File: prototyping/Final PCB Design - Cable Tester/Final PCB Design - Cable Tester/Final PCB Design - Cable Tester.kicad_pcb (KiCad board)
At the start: 2 copper layers, 86 x 54 mm, 41 parts, among them J17 Banana Jack, J20 SFML-110-02-L-D-A, J3 Debug Connection, J4 MEM2061-01-188-00-A_REVA, J5 Barrel Jack 9V, J6 Touchscreen HMI, Q1 2N3904, SW1 Rocker Switch, U1 AVR128DB64x-xMR, U2 LP2985-3.3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

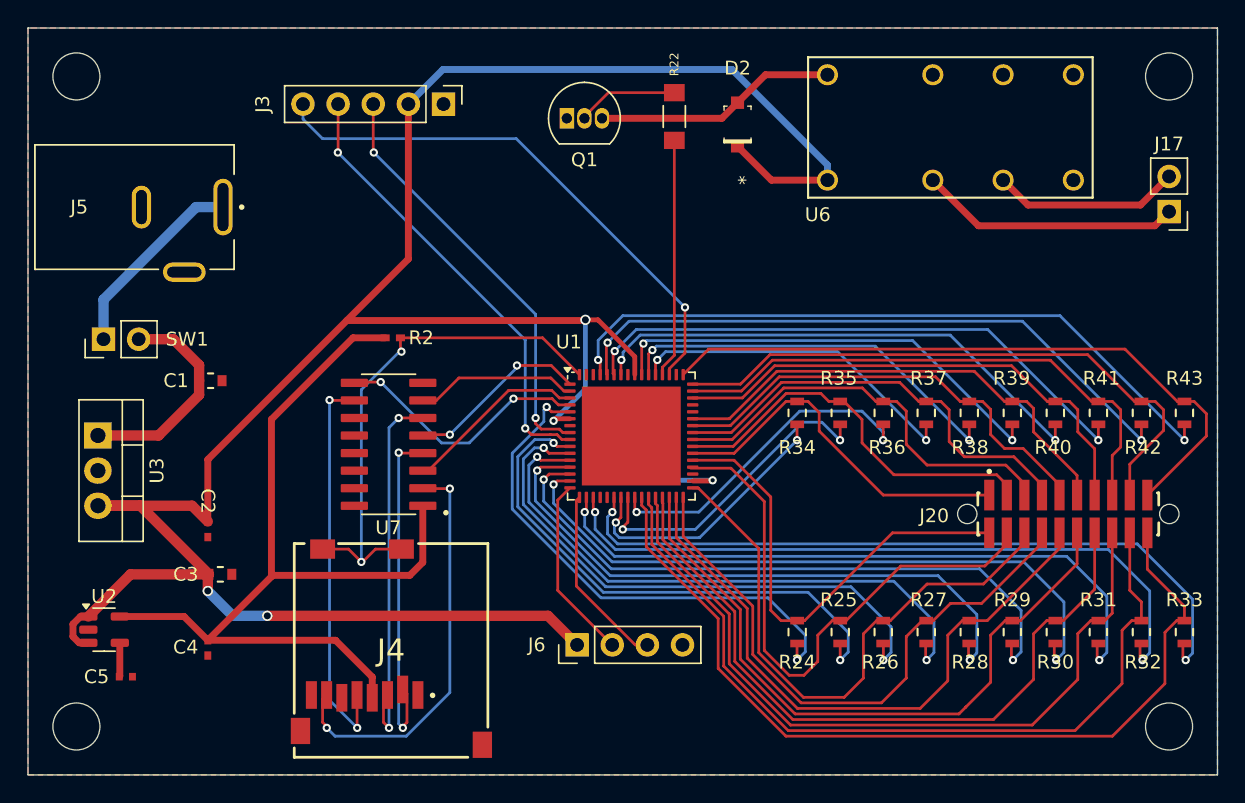
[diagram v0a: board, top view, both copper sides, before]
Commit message: Update - Final PCB to JLCPCB components
Added the JLCPCB Library and updated to equivalent components supplied by JLCPCB. Also updated the PCB traces to fit new components.
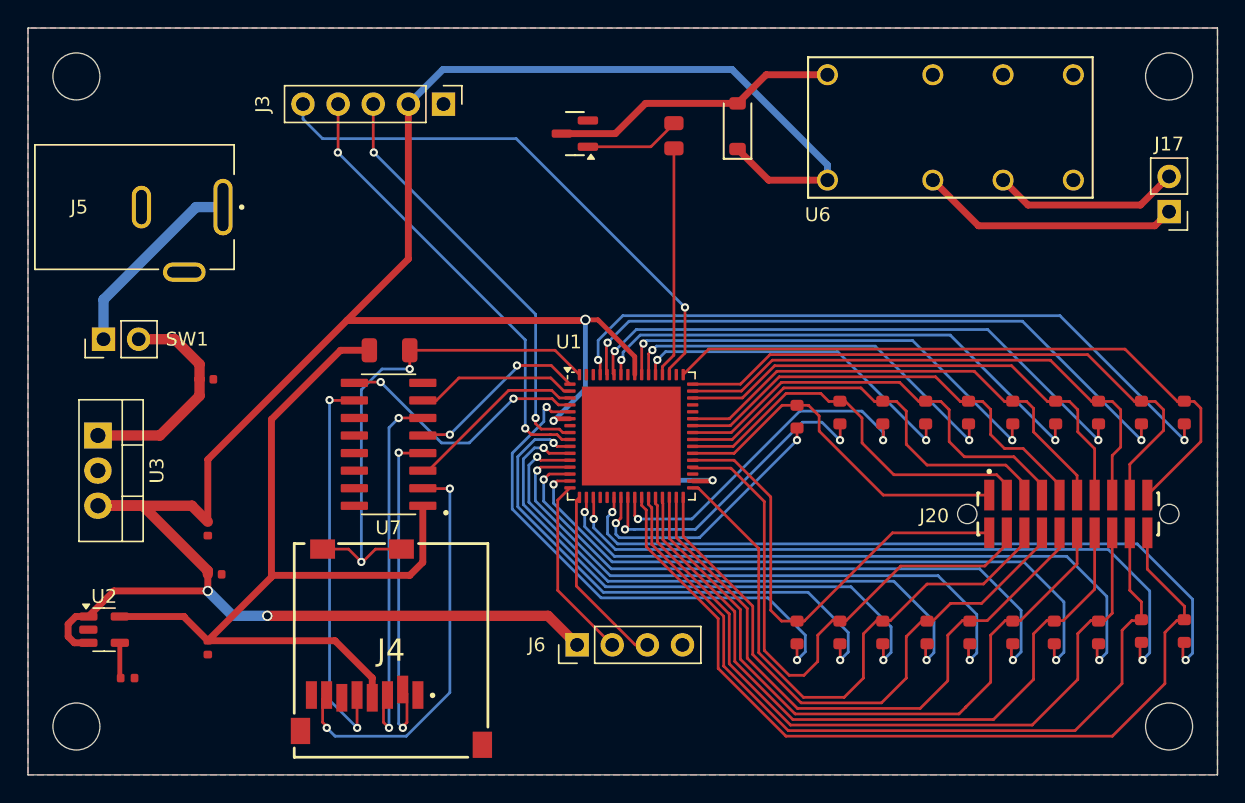
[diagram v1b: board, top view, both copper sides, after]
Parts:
- removed D2: 1N4148W-TP, digikey-footprints:SOD-123
- removed Q1: 2N3904, Package_TO_SOT_THT:TO-92_Inline
- removed R24, R25, R26, R27, R28, R29, R30, R31, R32, R33, R34, R35, R36, R37, R38, R39, R40, R41, R42, R43: 1kΩ ±0.1% 0.1W, KiCad Symbols and Footprints:RES_0816_SUS
- added D1: 1N4148W, PCM_JLCPCB:D_SOD-123, F.Cu at (142.8, 73.1)
- added Q2: MMBT3904, PCM_JLCPCB:Q_SOT-23, F.Cu at (131.0, 73.6)
- added R1: 10kΩ, PCM_JLCPCB:R_1206, F.Cu at (117.6, 89.3)
- added R10: 1kΩ ±0.1% 0.1W, PCM_JLCPCB:R_0603, F.Cu at (168.9, 109.7)
- added R11: 1kΩ ±0.1% 0.1W, PCM_JLCPCB:R_0603, F.Cu at (172.0, 109.6)
- added R12: 1kΩ ±0.1% 0.1W, PCM_JLCPCB:R_0603, F.Cu at (175.1, 109.6)
- added R13: 1kΩ ±0.1% 0.1W, PCM_JLCPCB:R_0603, F.Cu at (147.1, 94.1)
- added R14: 1kΩ ±0.1% 0.1W, PCM_JLCPCB:R_0603, F.Cu at (150.2, 93.8)
- added R15: 1kΩ ±0.1% 0.1W, PCM_JLCPCB:R_0603, F.Cu at (153.3, 93.8)
- added R16: 1kΩ ±0.1% 0.1W, PCM_JLCPCB:R_0603, F.Cu at (156.4, 93.8)
- added R17: 1kΩ ±0.1% 0.1W, PCM_JLCPCB:R_0603, F.Cu at (159.5, 93.8)
- added R18: 1kΩ ±0.1% 0.1W, PCM_JLCPCB:R_0603, F.Cu at (162.7, 93.8)
- added R19: 1kΩ ±0.1% 0.1W, PCM_JLCPCB:R_0603, F.Cu at (165.8, 93.8)
- added R20: 1kΩ ±0.1% 0.1W, PCM_JLCPCB:R_0603, F.Cu at (168.9, 93.8)
- added R21: 1kΩ ±0.1% 0.1W, PCM_JLCPCB:R_0603, F.Cu at (172.0, 93.8)
- added R3: 1kΩ ±0.1% 0.1W, PCM_JLCPCB:R_0603, F.Cu at (147.1, 109.7)
- added R4: 1kΩ ±0.1% 0.1W, PCM_JLCPCB:R_0603, F.Cu at (150.2, 109.7)
- added R5: 1kΩ ±0.1% 0.1W, PCM_JLCPCB:R_0603, F.Cu at (153.3, 109.7)
- added R6: 1kΩ ±0.1% 0.1W, PCM_JLCPCB:R_0603, F.Cu at (156.5, 109.7)
- added R7: 1kΩ ±0.1% 0.1W, PCM_JLCPCB:R_0603, F.Cu at (159.6, 109.7)
- added R8: 1kΩ ±0.1% 0.1W, PCM_JLCPCB:R_0603, F.Cu at (162.7, 109.7)
- added R9: 1kΩ ±0.1% 0.1W, PCM_JLCPCB:R_0603, F.Cu at (165.7, 109.7)
- C1, C3: value 1µF -> 1uF; footprint KiCad Symbols and Footprints:CAP_CL10_SAM -> PCM_JLCPCB:C_0402
- C2, C4: value 0.1µF -> 100nF; footprint KiCad Symbols and Footprints:CAP_CL05_SAM -> PCM_JLCPCB:C_0402
- C5: footprint KiCad Symbols and Footprints:CAPC10555_55N_KEM -> PCM_JLCPCB:C_0402
- J5: value Barrel Jack 9V -> 54-00129
- R2: value 10KΩ-0.25W -> 1.5kΩ; footprint KiCad Symbols and Footprints:RC0402N_PAN -> PCM_JLCPCB:R_0805
- R22: value 1.5kΩ 1/4W -> 1kΩ ±0.1% 0.1W; footprint KiCad Symbols and Footprints:RES_ERA8AEB152V -> PCM_JLCPCB:R_0603
- U2: value LP2985-3.3 -> LP2985-33DBVR
- U3: value LM7805_TO220 -> LM7805T
- moved R22 42.6 mm to (175.1, 93.8)
- moved R2 25.0 mm to (138.2, 73.8), turned to -90 degrees
- moved C3 0.41 mm to (105.0, 105.5)
- moved C1 0.32 mm to (104.4, 91.4)
- moved C5 0.16 mm to (98.7, 113.0)
- moved C2 0.05 mm to (104.5, 102.2)
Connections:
- R2 pad 1: +3.3V -> Net-(Q2-B)
- R2 pad 2: CD -> RSig
- R22 pad 1: RSig -> CTRL 20
- R22 pad 2: Net-(Q1-B) -> ADC 20
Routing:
- net Net-(Q1-B): track 7.57 -> 0.00 mm
- net Net-(Q2-B): track 0.00 -> 6.91 mm
- net Net-(Q2-C): track 17.6 -> 21.0 mm
- net +3.3V: track 65.6 -> 64.0 mm
- net CTRL 13: track 24.3 -> 25.0 mm
- net CD: track 38.0 -> 37.4 mm
- net RSig: track 17.3 -> 16.7 mm

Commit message: Updated - Final PCB - Fixed DRC issues
Fixed all errors, warnings, or issues in the DRC checker for the final PCB
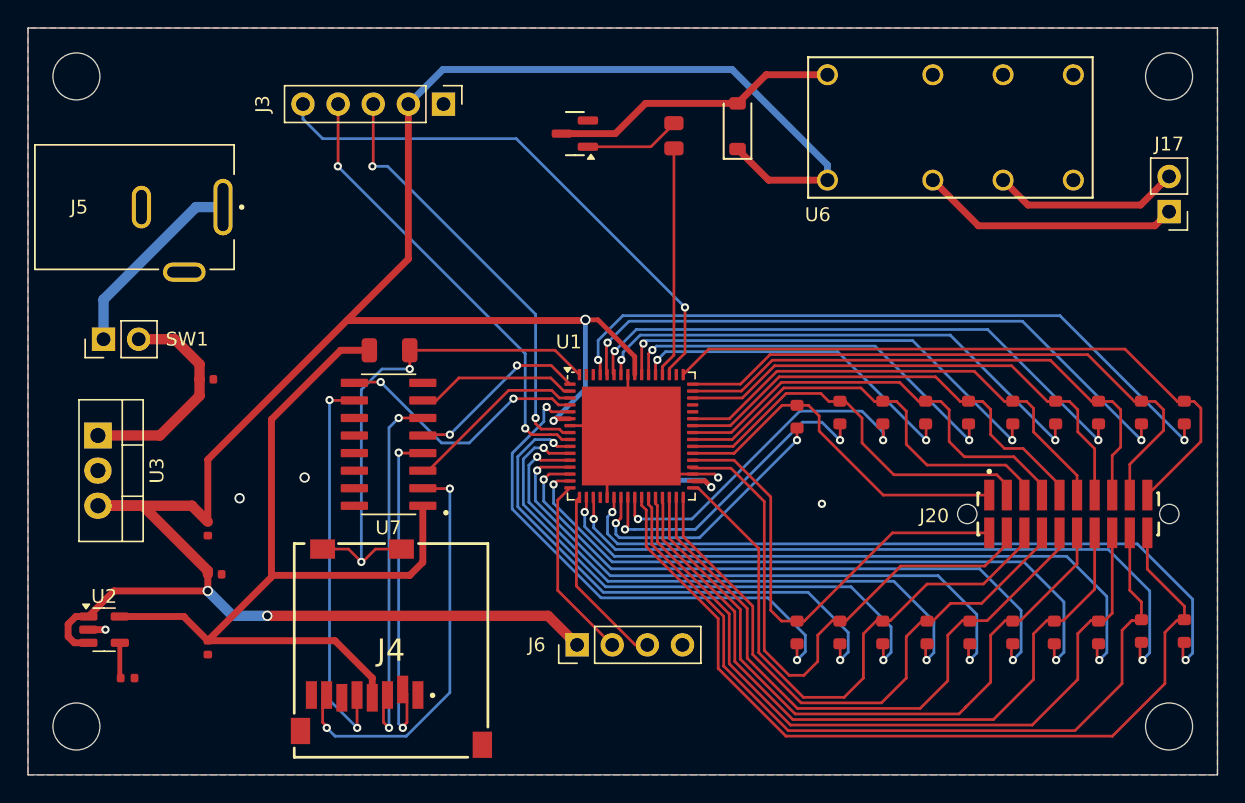
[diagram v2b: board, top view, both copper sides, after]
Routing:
- net GND: track 0.00 -> 23.2 mm, vias 0 -> 5
- net TxD: track 30.7 -> 31.4 mm
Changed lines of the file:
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@@
 	)
 	(segment
+		(start 140.45 98.75)
+		(end 139.5575 98.75)
+		(width 0.35)
+		(layer "F.Cu")
+		(net 3)
+	)
+	(segment
 		(start 99.796 100.54)
 		(end 104.5 105.244)
@@
 	)
 	(segment
-		(start 140.95 98.75)
-		(end 141 98.7)
+		(start 140.9 99.2)
+		(end 140.45 98.75)
 		(width 0.35)
 		(layer "F.Cu")
@@
 	)
 	(segment
-		(start 139.5575 98.75)
-		(end 140.95 98.75)
-		(width 0.35)
-		(layer "F.Cu")
-		(net 3)
-	)
-	(segment
 		(start 104.5 97.2)
 		(end 104.5 101.7)
@@
 	)
 	(via
-		(at 141 98.7)
+		(at 140.9 99.2)
 		(size 0.6)
 		(drill 0.3)
@@
 	)
 	(segment
+		(start 138.401 98.7)
+		(end 131.8 92.099)
+		(width 0.35)
+		(layer "B.Cu")
+		(net 3)
+	)
+	(segment
 		(start 106.3 108.5)
 		(end 104.5 106.7)
@@
 	)
 	(segment
-		(start 141 98.7)
-		(end 138.401 98.7)
+		(start 131.8 92.099)
+		(end 129.5 94.399)
 		(width 0.35)
 		(layer "B.Cu")
@@
 	)
 	(segment
-		(start 131.8 92.099)
-		(end 129.5 94.399)
+		(start 140.4 98.7)
+		(end 138.401 98.7)
 		(width 0.35)
 		(layer "B.Cu")
@@
 	)
 	(segment
-		(start 138.401 98.7)
-		(end 131.8 92.099)
+		(start 140.9 99.2)
+		(end 140.4 98.7)
 		(width 0.35)
 		(layer "B.Cu")
@@
 	)
 	(segment
-		(start 113.9 75)
-		(end 113.92 74.98)
+		(start 113.9 76)
+		(end 113.92 75.98)
 		(width 0.2)
 		(layer "F.Cu")
@@
 	)
 	(segment
-		(start 113.92 74.98)
-		(end 113.92 71.5)
+		(start 129.249265 95.4)
+		(end 127.9 95.4)
 		(width 0.2)
 		(layer "F.Cu")
@@
 	)
 	(segment
-		(start 129.249265 95.4)
-		(end 127.9 95.4)
+		(start 113.92 75.98)
+		(end 113.92 71.5)
 		(width 0.2)
 		(layer "F.Cu")
@@
 	)
 	(via
-		(at 113.9 75)
+		(at 113.9 76)
 		(size 0.6)
 		(drill 0.3)
@@
 	)
 	(segment
-		(start 127.450735 94.950735)
-		(end 127.450735 88.550735)
+		(start 127.450735 89.550735)
+		(end 127.450735 94.950735)
 		(width 0.2)
 		(layer "B.Cu")
@@
 	)
 	(segment
-		(start 127.450735 88.550735)
-		(end 113.9 75)
+		(start 113.9 76)
+		(end 127.450735 89.550735)
 		(width 0.2)
 		(layer "B.Cu")
@@
 	)
 	(segment
-		(start 116.5 75)
-		(end 116.46 74.96)
+		(start 116.4 76)
+		(end 116.46 75.94)
 		(width 0.2)
 		(layer "F.Cu")
@@
 	)
 	(segment
-		(start 128.599 94.999)
-		(end 128.2 94.6)
+		(start 116.46 75.94)
+		(end 116.46 71.5)
 		(width 0.2)
 		(layer "F.Cu")
@@
 	)
 	(segment
-		(start 130.6825 95.25)
-		(end 130.167043 95.25)
+		(start 128.599 94.999)
+		(end 128.2 94.6)
 		(width 0.2)
 		(layer "F.Cu")
@@
 	)
 	(segment
-		(start 116.46 74.96)
-		(end 116.46 71.5)
+		(start 130.6825 95.25)
+		(end 130.167043 95.25)
 		(width 0.2)
 		(layer "F.Cu")
@@
 	)
 	(via
-		(at 116.5 75)
+		(at 116.4 76)
 		(size 0.6)
 		(drill 0.3)
@@
 	)
 	(segment
-		(start 128.2 94.2)
+		(start 117.5 76)
 		(end 128.2 86.7)
 		(width 0.2)
@@
 	)
 	(segment
+		(start 116.4 76)
+		(end 117.5 76)
+		(width 0.2)
+		(layer "B.Cu")
+		(net 8)
+	)
+	(segment
 		(start 128.2 86.7)
-		(end 116.5 75)
+		(end 128.2 94.2)
 		(width 0.2)
 		(layer "B.Cu")
@@
 	)
 	(segment
+		(start 134.87 91.0625)
+		(end 134.87 95.25)
+		(width 0.2)
+		(layer "F.Cu")
+		(net 74)
+	)
+	(segment
+		(start 133.37 99.9375)
+		(end 133.37 97.25)
+		(width 0.2)
+		(layer "F.Cu")
+		(net 74)
+	)
+	(segment
+		(start 141.15 98.25)
+		(end 141.4 98.5)
+		(width 0.2)
+		(layer "F.Cu")
+		(net 74)
+	)
+	(segment
+		(start 139.5575 98.25)
+		(end 137.87 98.25)
+		(width 0.2)
+		(layer "F.Cu")
+		(net 74)
+	)
+	(segment
+		(start 139.5575 98.25)
+		(end 141.15 98.25)
+		(width 0.2)
+		(layer "F.Cu")
+		(net 74)
+	)
+	(segment
+		(start 95.8625 109.5)
+		(end 97.1 109.5)
+		(width 0.5)
+		(layer "F.Cu")
+		(net 74)
+	)
+	(segment
+		(start 130.6825 94.75)
+		(end 134.37 94.75)
+		(width 0.2)
+		(layer "F.Cu")
+		(net 74)
+	)
+	(segment
+		(start 134.37 94.75)
+		(end 135.12 95.5)
+		(width 0.2)
+		(layer "F.Cu")
+		(net 74)
+	)
+	(segment
+		(start 133.37 97.25)
+		(end 135.12 95.5)
+		(width 0.2)
+		(layer "F.Cu")
+		(net 74)
+	)
+	(segment
+		(start 134.87 95.25)
+		(end 135.12 95.5)
+		(width 0.2)
+		(layer "F.Cu")
+		(net 74)
+	)
+	(segment
+		(start 137.87 98.25)
+		(end 135.12 95.5)
+		(width 0.2)
+		(layer "F.Cu")
+		(net 74)
+	)
+	(via
+		(at 141.4 98.5)
+		(size 0.6)
+		(drill 0.3)
+		(layers "F.Cu" "B.Cu")
+		(free yes)
+		(net 74)
+	)
+	(via
+		(at 148.9 100.4)
+		(size 0.6)
+		(drill 0.3)
+		(layers "F.Cu" "B.Cu")
+		(free yes)
+		(net 74)
+	)
+	(via
+		(at 97.1 109.5)
+		(size 0.6)
+		(drill 0.3)
+		(layers "F.Cu" "B.Cu")
+		(free yes)
+		(net 74)
+	)
+	(via
+		(at 111.5 98.5)
+		(size 0.75)
+		(drill 0.5)
+		(layers "F.Cu" "B.Cu")
+		(free yes)
+		(net 74)
+	)
+	(via
+		(at 106.8 100)
+		(size 0.75)
+		(drill 0.5)
+		(layers "F.Cu" "B.Cu")
+		(free yes)
+		(net 74)
+	)
+	(segment

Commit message: Update - Final PCB
Changed the Samtec connector and made minor adjustments
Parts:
- removed J20: SFML-110-02-L-D-A, KiCad Symbols and Footprints:SAMTEC_SFML-110-02-L-D-A
- added J1: SFML-110-T1-S-D, KiCad Symbols and Footprints:SAMTEC_SFML-110-T1-S-D, F.Cu at (166.7, 101.0)
- SW1: value Rocker Switch -> 1x2 Pin header
- renumbered Q2 to Q1, U7 to U4
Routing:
- net ADC 5: track 45.7 -> 46.5 mm
- net ADC 7: track 51.7 -> 52.5 mm
- net ADC 4: track 43.1 -> 43.9 mm
- net ADC 2: track 41.2 -> 42.1 mm
- net ADC 8: track 54.9 -> 55.7 mm
- net ADC 3: track 41.9 -> 42.7 mm
- net ADC 6: track 48.5 -> 49.4 mm
- net ADC 9: track 58.8 -> 59.6 mm
- net ADC 10: track 63.5 -> 64.2 mm
- net TxD: track 31.4 -> 30.8 mm
- net ADC 20: track 47.9 -> 48.5 mm
- net ADC 19: track 43.8 -> 44.4 mm
- net ADC 18: track 39.8 -> 40.4 mm
- net ADC 14: track 31.9 -> 32.5 mm
- net ADC 15: track 33.0 -> 33.6 mm
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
